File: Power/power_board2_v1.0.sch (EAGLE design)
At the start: 103 parts, among them J0_VLINE_CONN 172648-0102, J1_B3_CONN1 105313-1102, J1_B3_CONN2 105313-1102, J3_9VNO1_CONN 43650-0212, J4_9VNO2_CONN 43650-0212, Q2 FQD11P06TM

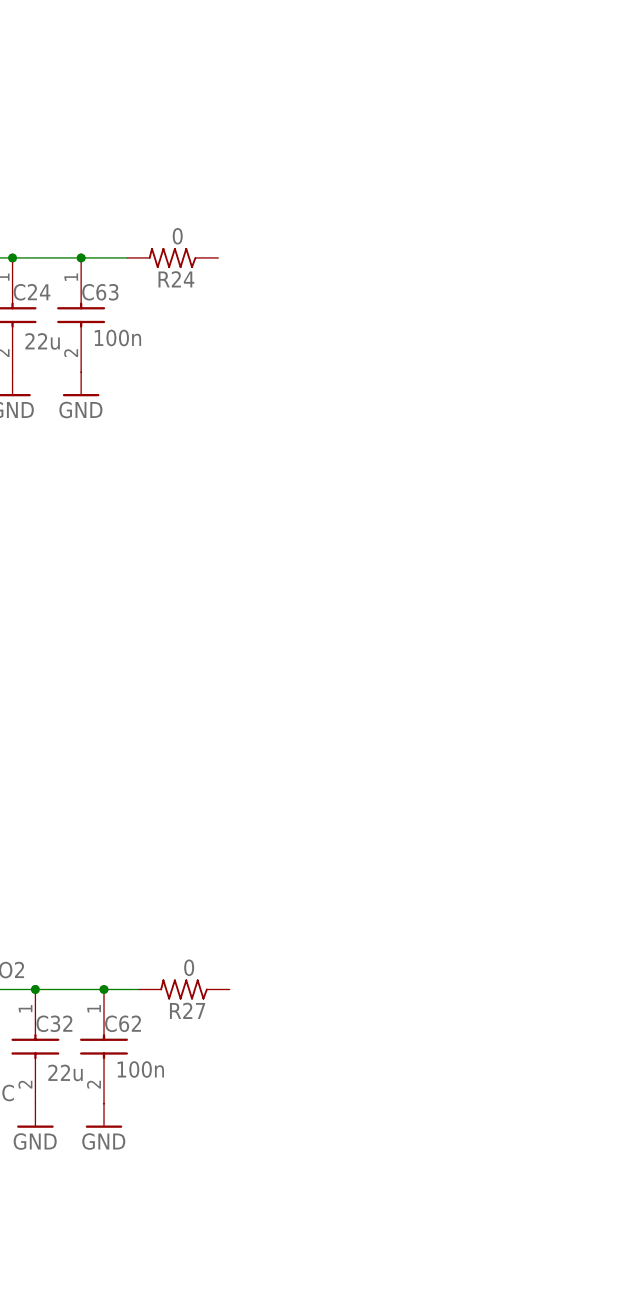
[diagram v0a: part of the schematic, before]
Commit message: Cleaned up the Payload Power Board sch and brd and am almost done with the Voltage Lines Board sch and brd
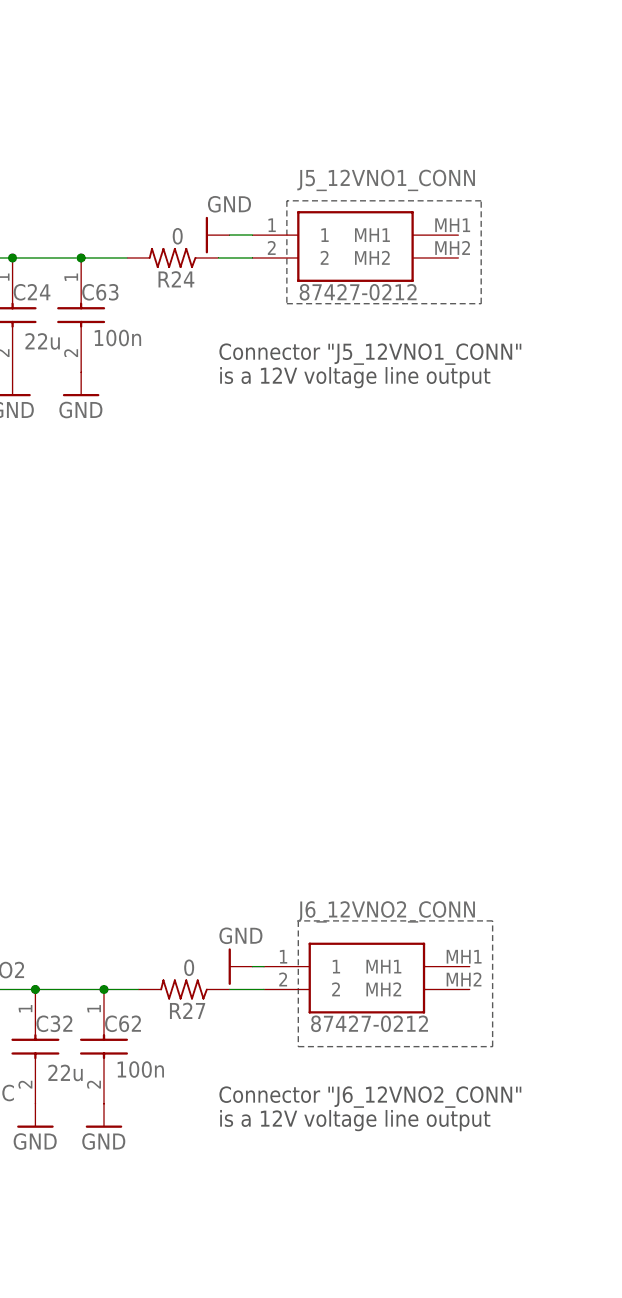
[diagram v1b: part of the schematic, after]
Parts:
- added J5_12VNO1_CONN, J6_12VNO2_CONN: 87427-0212, 87427-0212:87427-0212
- C24, C32: value 50.8u -> 22u
- renumbered J1_B3_CONN1 to J1_5VNO1_CONN, J1_B3_CONN2 to J2_5VNO2_CONN
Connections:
- net N$10 renamed CBOOST_5VNO1
- net N$11 renamed CBOOST_9VNO1
- net N$12 renamed V_9VNO1_0
- net N$2 renamed CBOOST_12VNO2
- net N$3 renamed CBOOST_12VNO1
- net N$7 renamed CBOOST_5VNO2
- net N$8 renamed V_9VNO2_0
- net N$9 renamed CBOOST_9VNO2
- new net V_12VNO1_0: J5_12VNO1_CONN.2, R24.1
- new net V_12VNO2_0: J6_12VNO2_CONN.2, R27.1
- net GND: now also J5_12VNO1_CONN.1, J6_12VNO2_CONN.1
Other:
- note added: "Connector "J5_12VNO1_CONN" is a 12V voltage line output"
- note added: "Connector "J6_12VNO2_CONN" is a 12V voltage line output"
